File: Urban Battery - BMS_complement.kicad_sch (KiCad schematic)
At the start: 38 parts, among them J1 BMS IO, J10 E-Stop, J11 Contactor Connector, J12 Thermistor, J13 Thermistor, J14 Thermistor, J2 OLED Header, J3 CAN Connector, J4 CAN Connector, J5 Charge Connector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

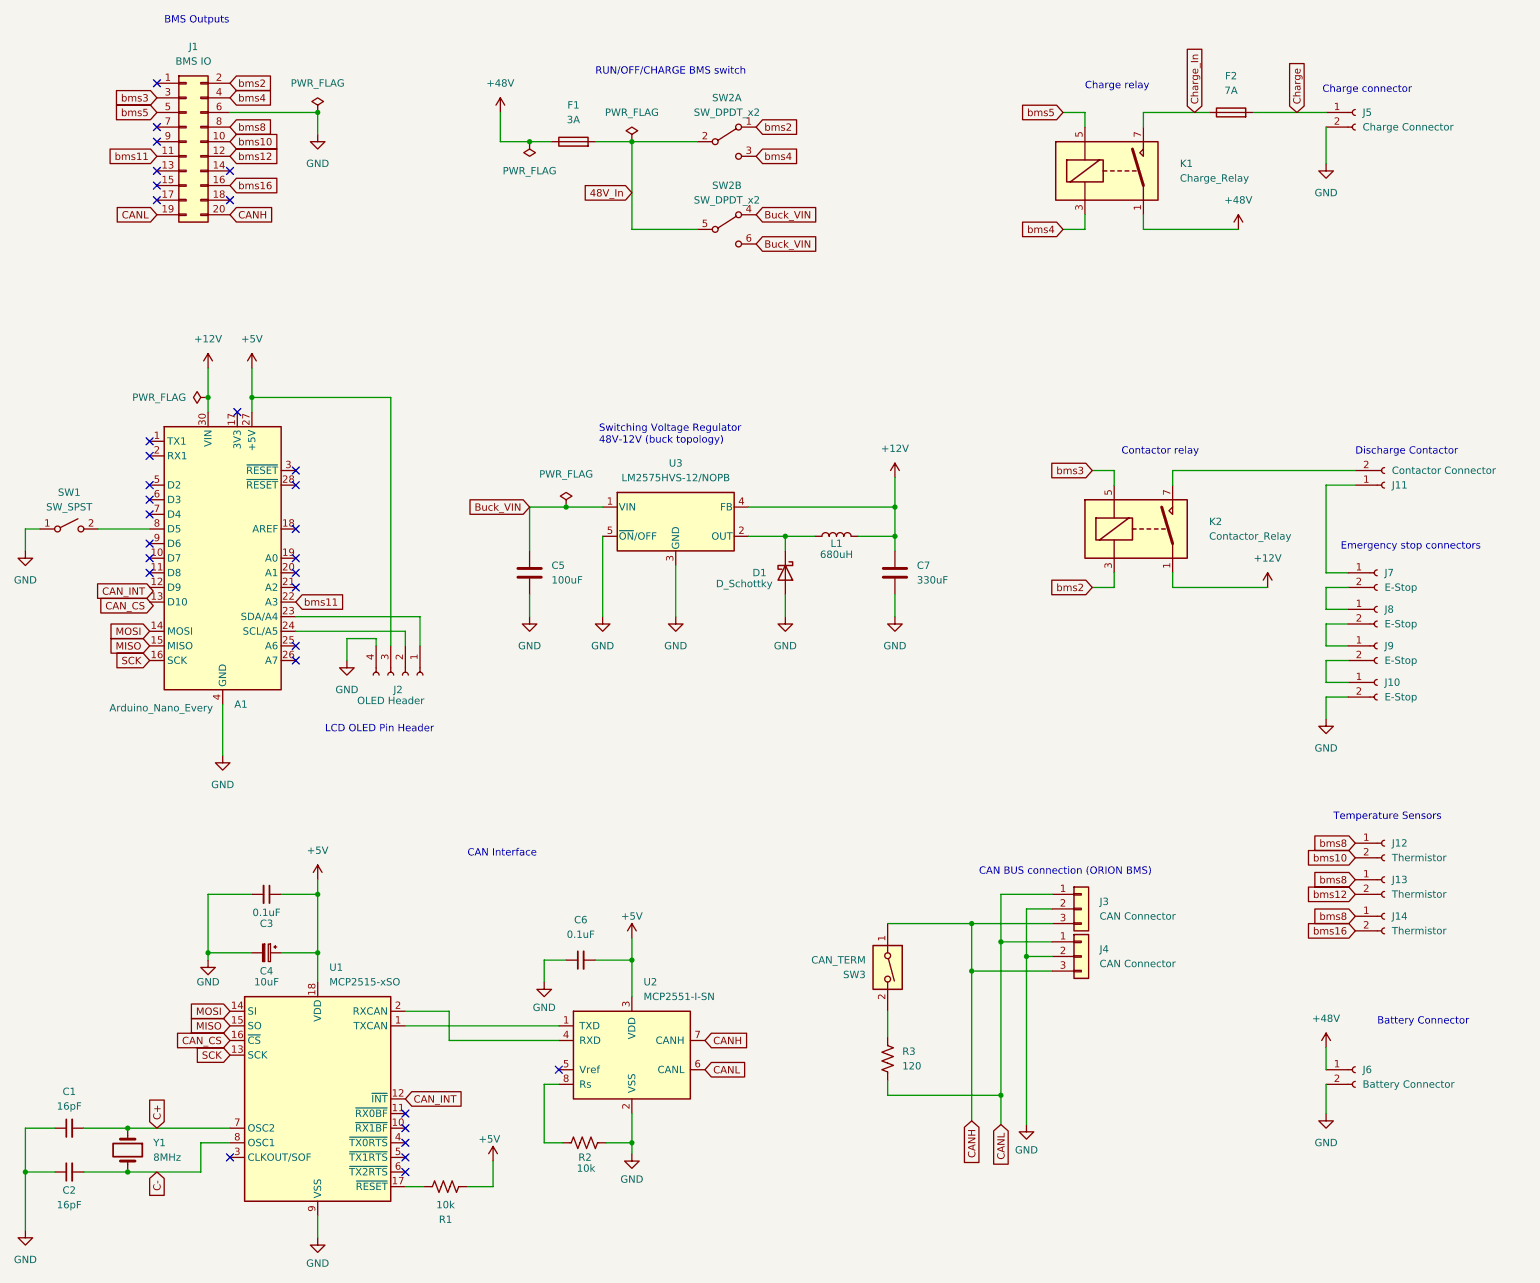
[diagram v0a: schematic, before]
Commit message: Updated C4, added differential pairs to CAN
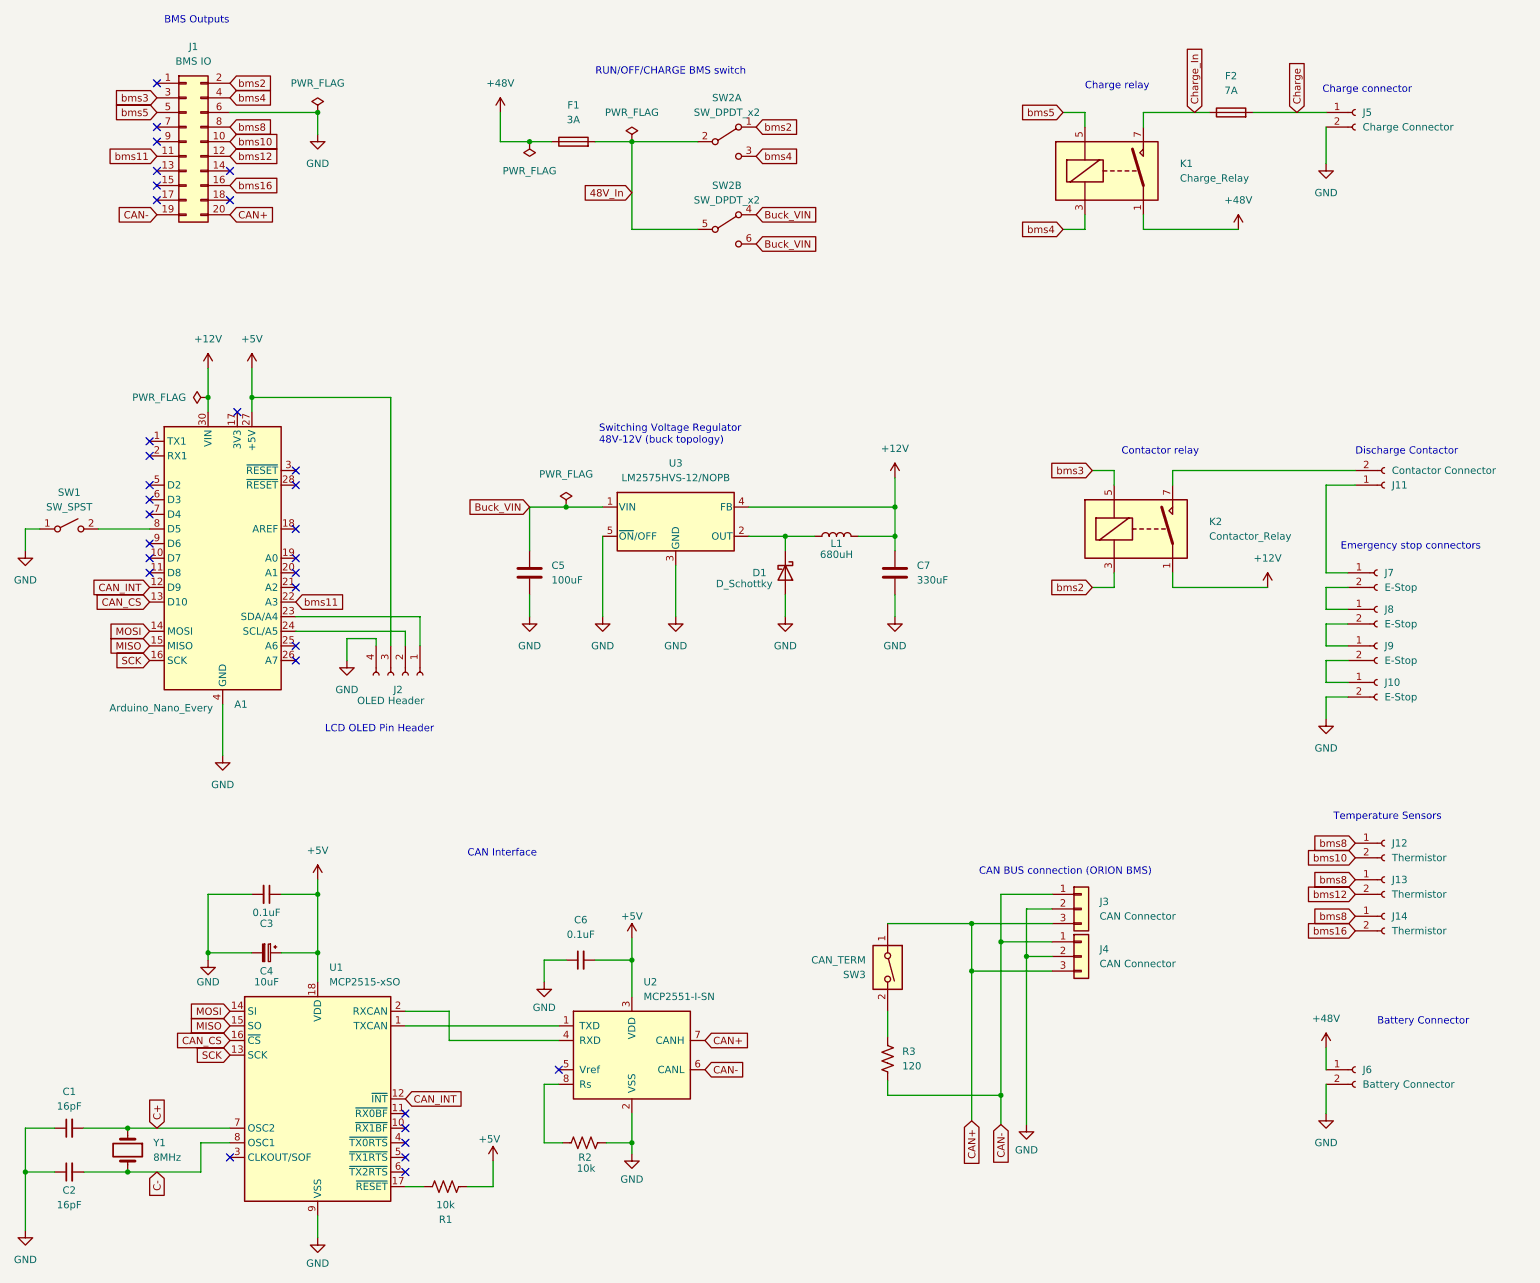
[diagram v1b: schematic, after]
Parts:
- C4: footprint Capacitor_SMD:C_0805_2012Metric_Pad1.18x1.45mm_HandSolder -> Capacitor_THT:CP_Radial_D10.0mm_P5.00mm
- K1, K2: footprint Relay_THT:Relay_SPST_StandexMeder_SIL_Form1A -> BMS_Custom_Footprints:Relay_RT334048
- L1: footprint BMS_Custom_Footprints:PE-52629NL -> BMS_Custom_Footprints:Inductor_PE-52629NL
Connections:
- net CAN_CS: now also A1.13 (D10)
- net CAN_INT: now also A1.12 (D9)
- net CANH renamed CAN+
- net CANL renamed CAN-

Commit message: Updated silkscreen, added test points
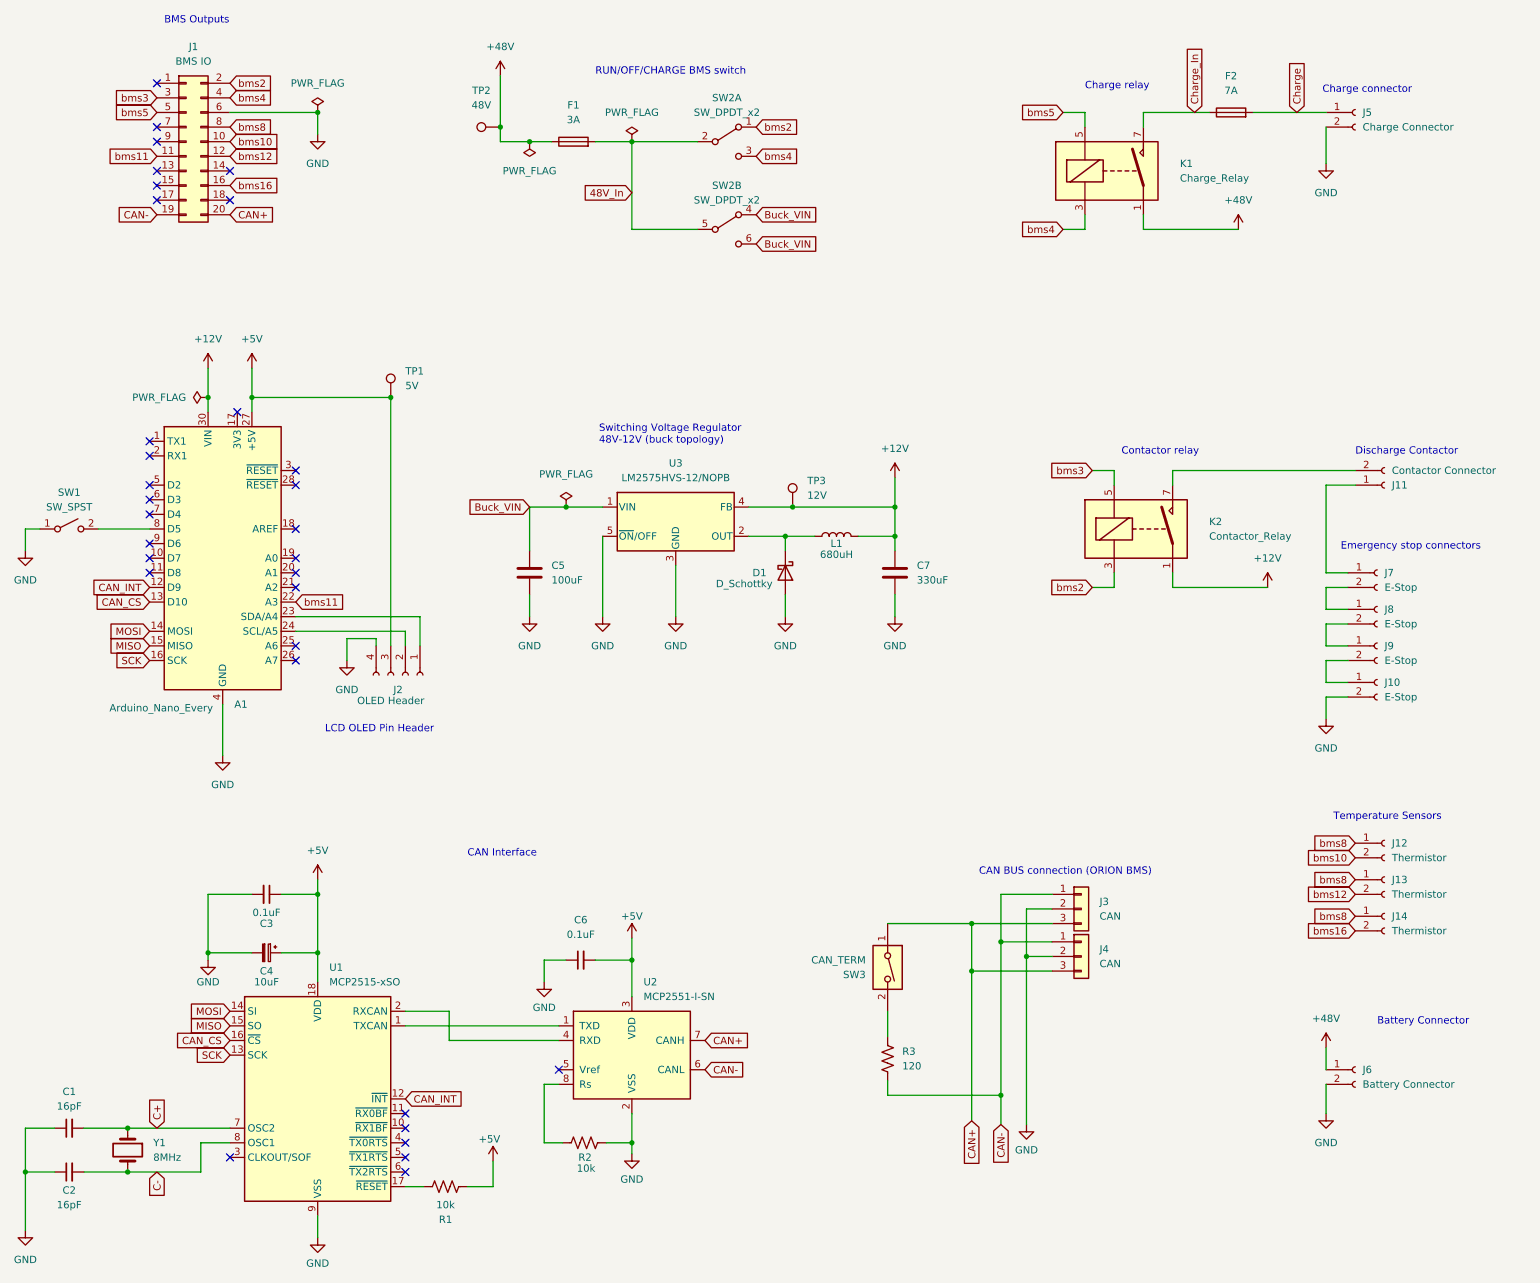
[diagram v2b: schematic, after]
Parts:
- added TP1: 5V, TestPoint:TestPoint_Pad_2.0x2.0mm, symbol Connector:TestPoint
- added TP2: 48V, TestPoint:TestPoint_Pad_2.0x2.0mm, symbol Connector:TestPoint
- added TP3: 12V, TestPoint:TestPoint_Pad_2.0x2.0mm, symbol Connector:TestPoint
- J3, J4: value CAN Connector -> CAN
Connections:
- net +12V: now also TP3.1
- net +48V: now also TP2.1
- net +5V: now also TP1.1
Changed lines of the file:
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@@
   (junction (at 76.2 194.31) (diameter 0) (color 0 0 0 0)
   )
+  (junction (at 158.75 127) (diameter 0) (color 0 0 0 0)
+  )
   (junction (at 189.865 199.39) (diameter 0) (color 0 0 0 0)
   )
@@
   (junction (at 57.15 204.47) (diameter 0) (color 0 0 0 0)
   )
+  (junction (at 88.9 107.95) (diameter 0) (color 0 0 0 0)
+  )
   (junction (at 194.945 229.235) (diameter 0) (color 0 0 0 0)
   )
@@
   )
   (junction (at 119.38 127) (diameter 0) (color 0 0 0 0)
+  )
+  (junction (at 107.95 60.96) (diameter 0) (color 0 0 0 0)
   )
   (junction (at 157.48 132.08) (diameter 0) (color 0 0 0 0)
@@
     (stroke (width 0) (type default) (color 0 0 0 0))
   )
-  (wire (pts (xy 107.95 58.42) (xy 107.95 63.5))
+  (wire (pts (xy 107.95 60.96) (xy 107.95 63.5))
     (stroke (width 0) (type default) (color 0 0 0 0))
   )
@@
     (stroke (width 0) (type default) (color 0 0 0 0))
   )
+  (wire (pts (xy 158.75 127) (xy 176.53 127))
+    (stroke (width 0) (type default) (color 0 0 0 0))
+  )
   (wire (pts (xy 25.4 242.57) (xy 30.48 242.57))
     (stroke (width 0) (type default) (color 0 0 0 0))
@@
     (stroke (width 0) (type default) (color 0 0 0 0))
   )
-  (wire (pts (xy 151.13 127) (xy 176.53 127))
+  (wire (pts (xy 151.13 127) (xy 158.75 127))
     (stroke (width 0) (type default) (color 0 0 0 0))
   )
@@
   )
   (wire (pts (xy 64.77 107.95) (xy 64.77 110.49))
+    (stroke (width 0) (type default) (color 0 0 0 0))
+  )
+  (wire (pts (xy 107.95 52.07) (xy 107.95 60.96))
     (stroke (width 0) (type default) (color 0 0 0 0))
   )
@@
     (pin "1")
     (pin "2")
+  )
+  (symbol (lib_id "Connector:TestPoint") (at 107.95 60.96 90) (unit 1)
+    (in_bom yes) (on_board yes) (fields_autoplaced)
+    (property "Reference" "TP2" (id 0) (at 104.648 54.61 90))
+    (property "Value" "48V" (id 1) (at 104.648 57.15 90))
+    (property "Footprint" "TestPoint:TestPoint_Pad_2.0x2.0mm" (id 2) (at 107.95 55.88 0)
+      (effects (font (size 1.27 1.27)) hide)
+    )
+    (property "Datasheet" "~" (id 3) (at 107.95 55.88 0)
+      (effects (font (size 1.27 1.27)) hide)
+    )
+    (pin "1")
   )
   (symbol (lib_id "power:GND") (at 251.46 67.31 0) (unit 1)
@@
     (pin "5")
     (pin "6")
+  )
+  (symbol (lib_id "Connector:TestPoint") (at 158.75 127 0) (unit 1)
+    (in_bom yes) (on_board yes) (fields_autoplaced)
+    (property "Reference" "TP3" (id 0) (at 161.29 122.4279 0)
+      (effects (font (size 1.27 1.27)) (justify left))
+    )
+    (property "Value" "12V" (id 1) (at 161.29 124.9679 0)
+      (effects (font (size 1.27 1.27)) (justify left))
+    )
+    (property "Footprint" "TestPoint:TestPoint_Pad_2.0x2.0mm" (id 2) (at 163.83 127 0)
+      (effects (font (size 1.27 1.27)) hide)
+    )
+    (property "Datasheet" "~" (id 3) (at 163.83 127 0)
+      (effects (font (size 1.27 1.27)) hide)
+    )
+    (pin "1")
   )
   (symbol (lib_id "power:+5V") (at 106.68 240.665 0) (unit 1)
@@
       (effects (font (size 1.27 1.27)) (justify left))
     )
-    (property "Value" "CAN Connector" (id 1) (at 212.09 206.3749 0)
+    (property "Value" "CAN" (id 1) (at 212.09 206.3749 0)
       (effects (font (size 1.27 1.27)) (justify left))
     )
@@
       (effects (font (size 1.27 1.27)) (justify left))
     )
-    (property "Value" "CAN Connector" (id 1) (at 212.09 198.1199 0)
+    (property "Value" "CAN" (id 1) (at 212.09 198.1199 0)
       (effects (font (size 1.27 1.27)) (justify left))
     )
@@
     (pin "2")
   )
+  (symbol (lib_id "Connector:TestPoint") (at 88.9 107.95 0) (unit 1)
+    (in_bom yes) (on_board yes) (fields_autoplaced)
+    (property "Reference" "TP1" (id 0) (at 91.44 103.3779 0)
+      (effects (font (size 1.27 1.27)) (justify left))
+    )
+    (property "Value" "5V" (id 1) (at 91.44 105.9179 0)
+      (effects (font (size 1.27 1.27)) (justify left))
+    )
+    (property "Footprint" "TestPoint:TestPoint_Pad_2.0x2.0mm" (id 2) (at 93.98 107.95 0)
+      (effects (font (size 1.27 1.27)) hide)
+    )
+    (property "Datasheet" "~" (id 3) (at 93.98 107.95 0)
+      (effects (font (size 1.27 1.27)) hide)
+    )
+    (pin "1")
+  )
   (symbol (lib_id "power:PWR_FLAG") (at 119.38 127 0) (unit 1)
     (in_bom yes) (on_board yes) (fields_autoplaced)
@@
     (pin "1")
   )
-  (symbol (lib_id "power:+48V") (at 107.95 58.42 0) (unit 1)
-    (in_bom yes) (on_board yes)
-    (property "Reference" "#PWR012" (id 0) (at 107.95 62.23 0)
-      (effects (font (size 1.27 1.27)) hide)
-    )
-    (property "Value" "+48V" (id 1) (at 107.95 53.34 0))
-    (property "Footprint" "" (id 2) (at 107.95 58.42 0)
-      (effects (font (size 1.27 1.27)) hide)
-    )
-    (property "Datasheet" "" (id 3) (at 107.95 58.42 0)
+  (symbol (lib_id "power:+48V") (at 107.95 52.07 0) (unit 1)
+    (in_bom yes) (on_board yes)
+    (property "Reference" "#PWR012" (id 0) (at 107.95 55.88 0)
+      (effects (font (size 1.27 1.27)) hide)
+    )
+    (property "Value" "+48V" (id 1) (at 107.95 46.99 0))
+    (property "Footprint" "" (id 2) (at 107.95 52.07 0)
+      (effects (font (size 1.27 1.27)) hide)
+    )
+    (property "Datasheet" "" (id 3) (at 107.95 52.07 0)
       (effects (font (size 1.27 1.27)) hide)
     )
@@
     )
     (path "/a6ca1e7c-ab00-4766-b53d-a23ae079aec8"
-      (reference "J3") (unit 1) (value "CAN Connector") (footprint "BMS_Custom_Footprints:molex-sl-1x03-horizontal")
+      (reference "J3") (unit 1) (value "CAN") (footprint "BMS_Custom_Footprints:molex-sl-1x03-horizontal")
     )
     (path "/80ad110c-6531-499e-a391-2a4cd12237d8"
-      (reference "J4") (unit 1) (value "CAN Connector") (footprint "BMS_Custom_Footprints:molex-sl-1x03-horizontal")
+      (reference "J4") (unit 1) (value "CAN") (footprint "BMS_Custom_Footprints:molex-sl-1x03-horizontal")
     )
     (path "/7c8b5bee-9709-44ed-b549-ea2a8e264dfd"
@@
       (reference "SW3") (unit 1) (value "CAN_TERM") (footprint "Connector_PinHeader_2.54mm:PinHeader_1x02_P2.54mm_Horizontal")
     )
+    (path "/eef32152-f9dc-4649-9d55-9489cf921ed2"
+      (reference "TP1") (unit 1) (value "5V") (footprint "TestPoint:TestPoint_Pad_2.0x2.0mm")
+    )
+    (path "/0f317ba4-2b41-44a3-bd03-0cb72b4ae684"
+      (reference "TP2") (unit 1) (value "48V") (footprint "TestPoint:TestPoint_Pad_2.0x2.0mm")
+    )
+    (path "/28186176-f9e2-42a7-ac87-3d353cd41ccb"
+      (reference "TP3") (unit 1) (value "12V") (footprint "TestPoint:TestPoint_Pad_2.0x2.0mm")
+    )
     (path "/38a517b7-e3ff-44bb-944f-e8a6ce592fe9"
